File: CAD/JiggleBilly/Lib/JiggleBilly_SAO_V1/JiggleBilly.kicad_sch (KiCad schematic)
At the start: 5 parts, among them X1 Badgelife_sao_connector_v169b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

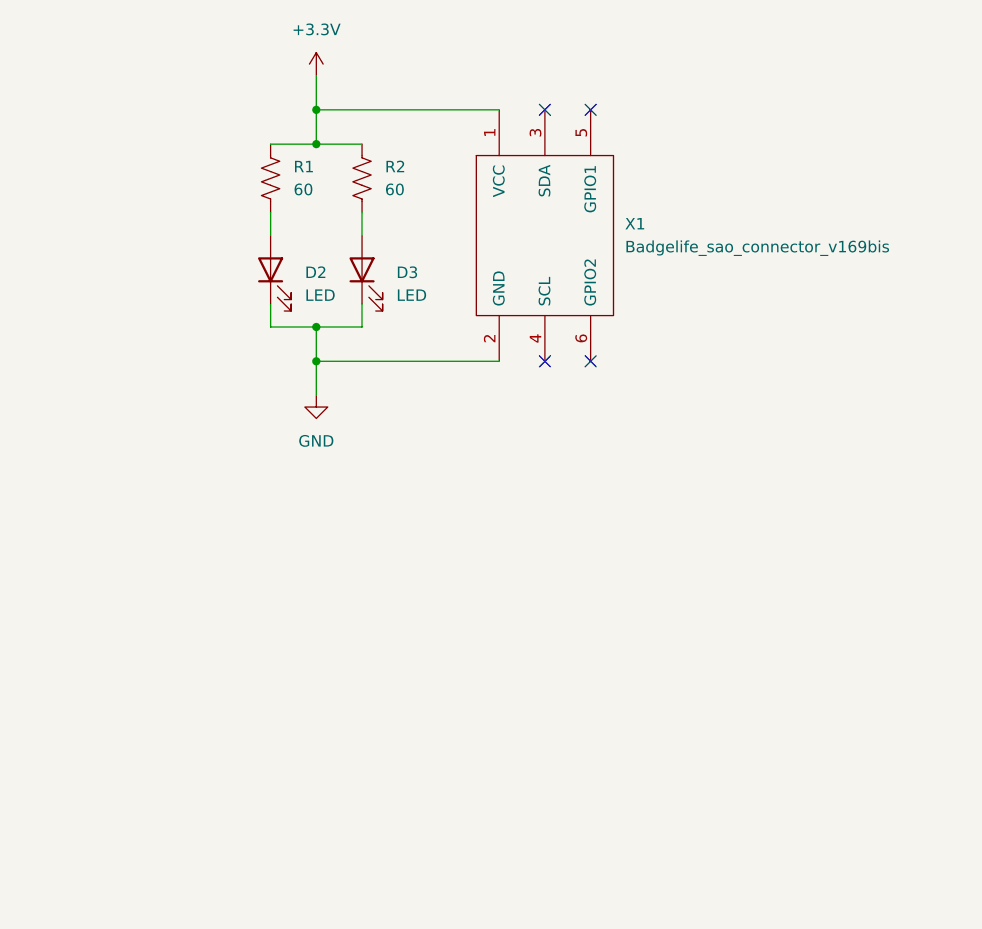
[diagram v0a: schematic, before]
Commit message: Update part info
Updated part info for BOM generaton
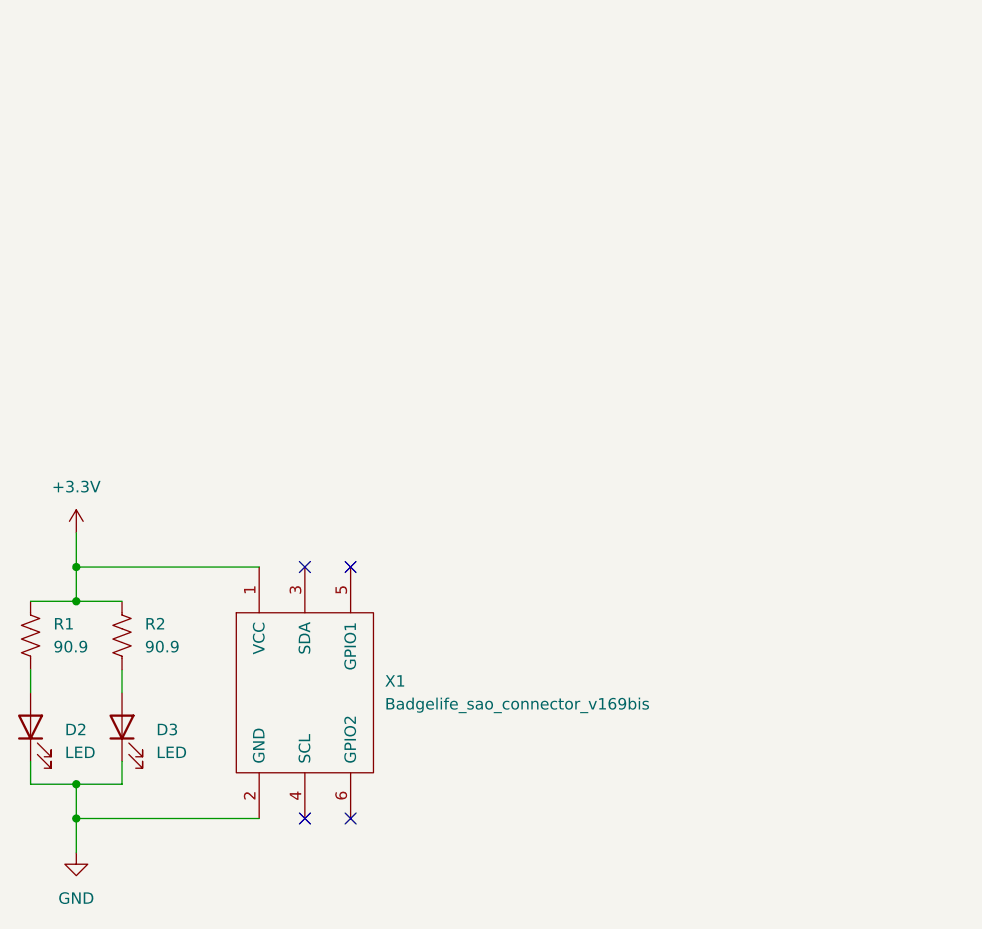
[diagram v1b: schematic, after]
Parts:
- D2, D3: MFG (none) -> SunLED; MPN (none) -> XZVG45WT-9; Vendor PN 1 (none) -> XZVG45WT-9; Vendor1 (none) -> DigiKey
- R1, R2: value 60 -> 90.9; MFG YAGEO -> Stackpole Electronics Inc; MPN RC0805JR-0756RL -> RMCF0805FT90R9; Vendor 2 Digikey -> (none); Vendor PN 1 C113305 -> RMCF0805FT90R9CT-ND; Vendor PN 2 311-56ARCT-ND -> (none); Vendor1 LCSC -> Digikey
- X1: MFG (none) -> Cvilux USA; MPN (none) -> CH87062V200; Vendor PN 1 (none) -> 2987-CH87062V200-ND; Vendor1 (none) -> Digikey
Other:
- moved on the sheet: D2, R1, X1
